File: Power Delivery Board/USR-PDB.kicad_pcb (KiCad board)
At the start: 2 copper layers, 110 x 150 mm, 40 parts, among them U1 XT90, U10 Anderson PP45 Vert. 2x1, U11 Anderson PP45 Vert. 2x1, U12 Anderson PP45 Vert. 2x1, U13 TL2575HV-05IKV, U14 MCP3002-I/P, U2 Anderson PP45 Vert. 2x1, U3 Anderson PP45 Vert. 2x1, U4 Anderson PP45 Vert. 2x1, U5 Anderson PP45 Vert. 2x1, U6 Anderson PP45 Vert. 2x1, U7 LM2676T-12_NOPB

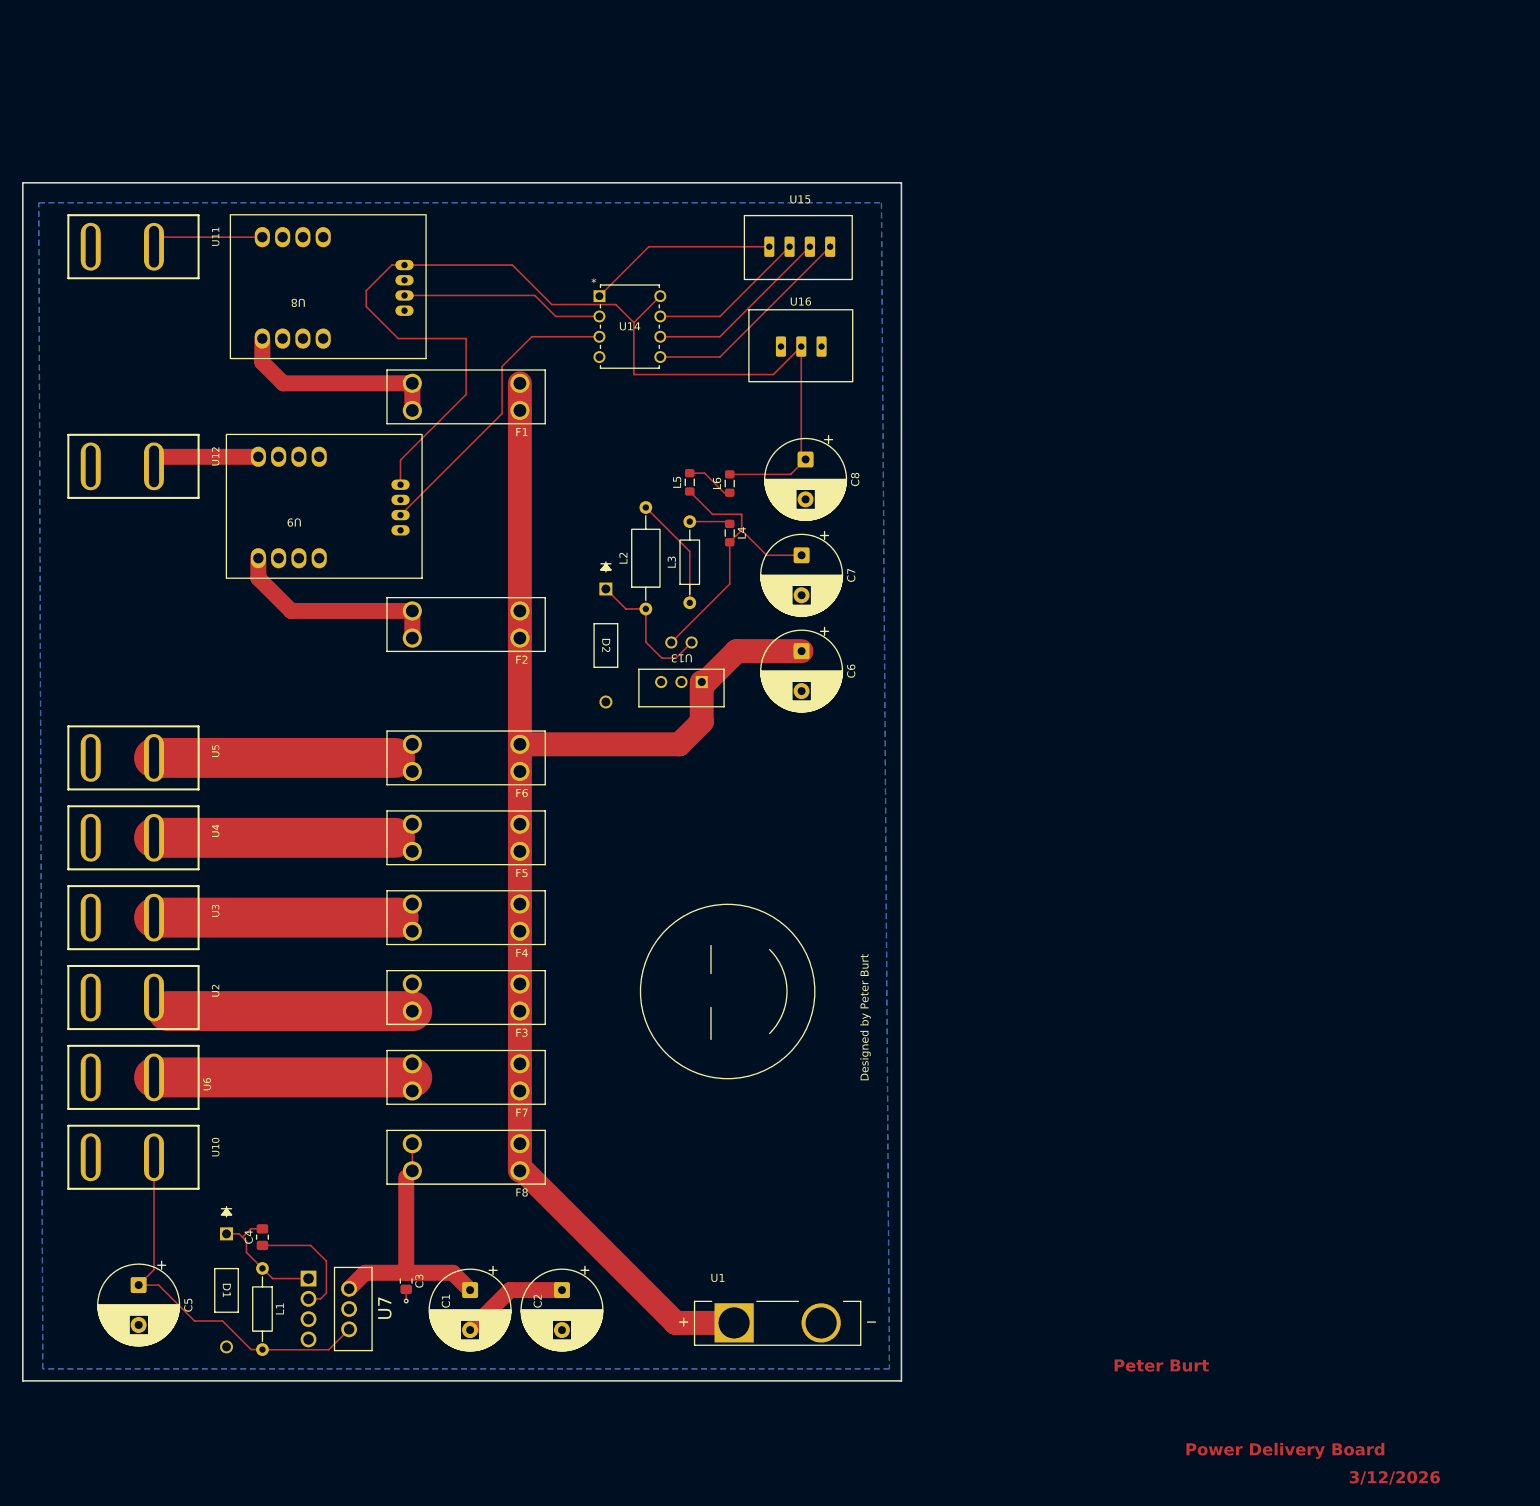
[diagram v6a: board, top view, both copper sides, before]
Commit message: Update PDB with easier-to-obtain components
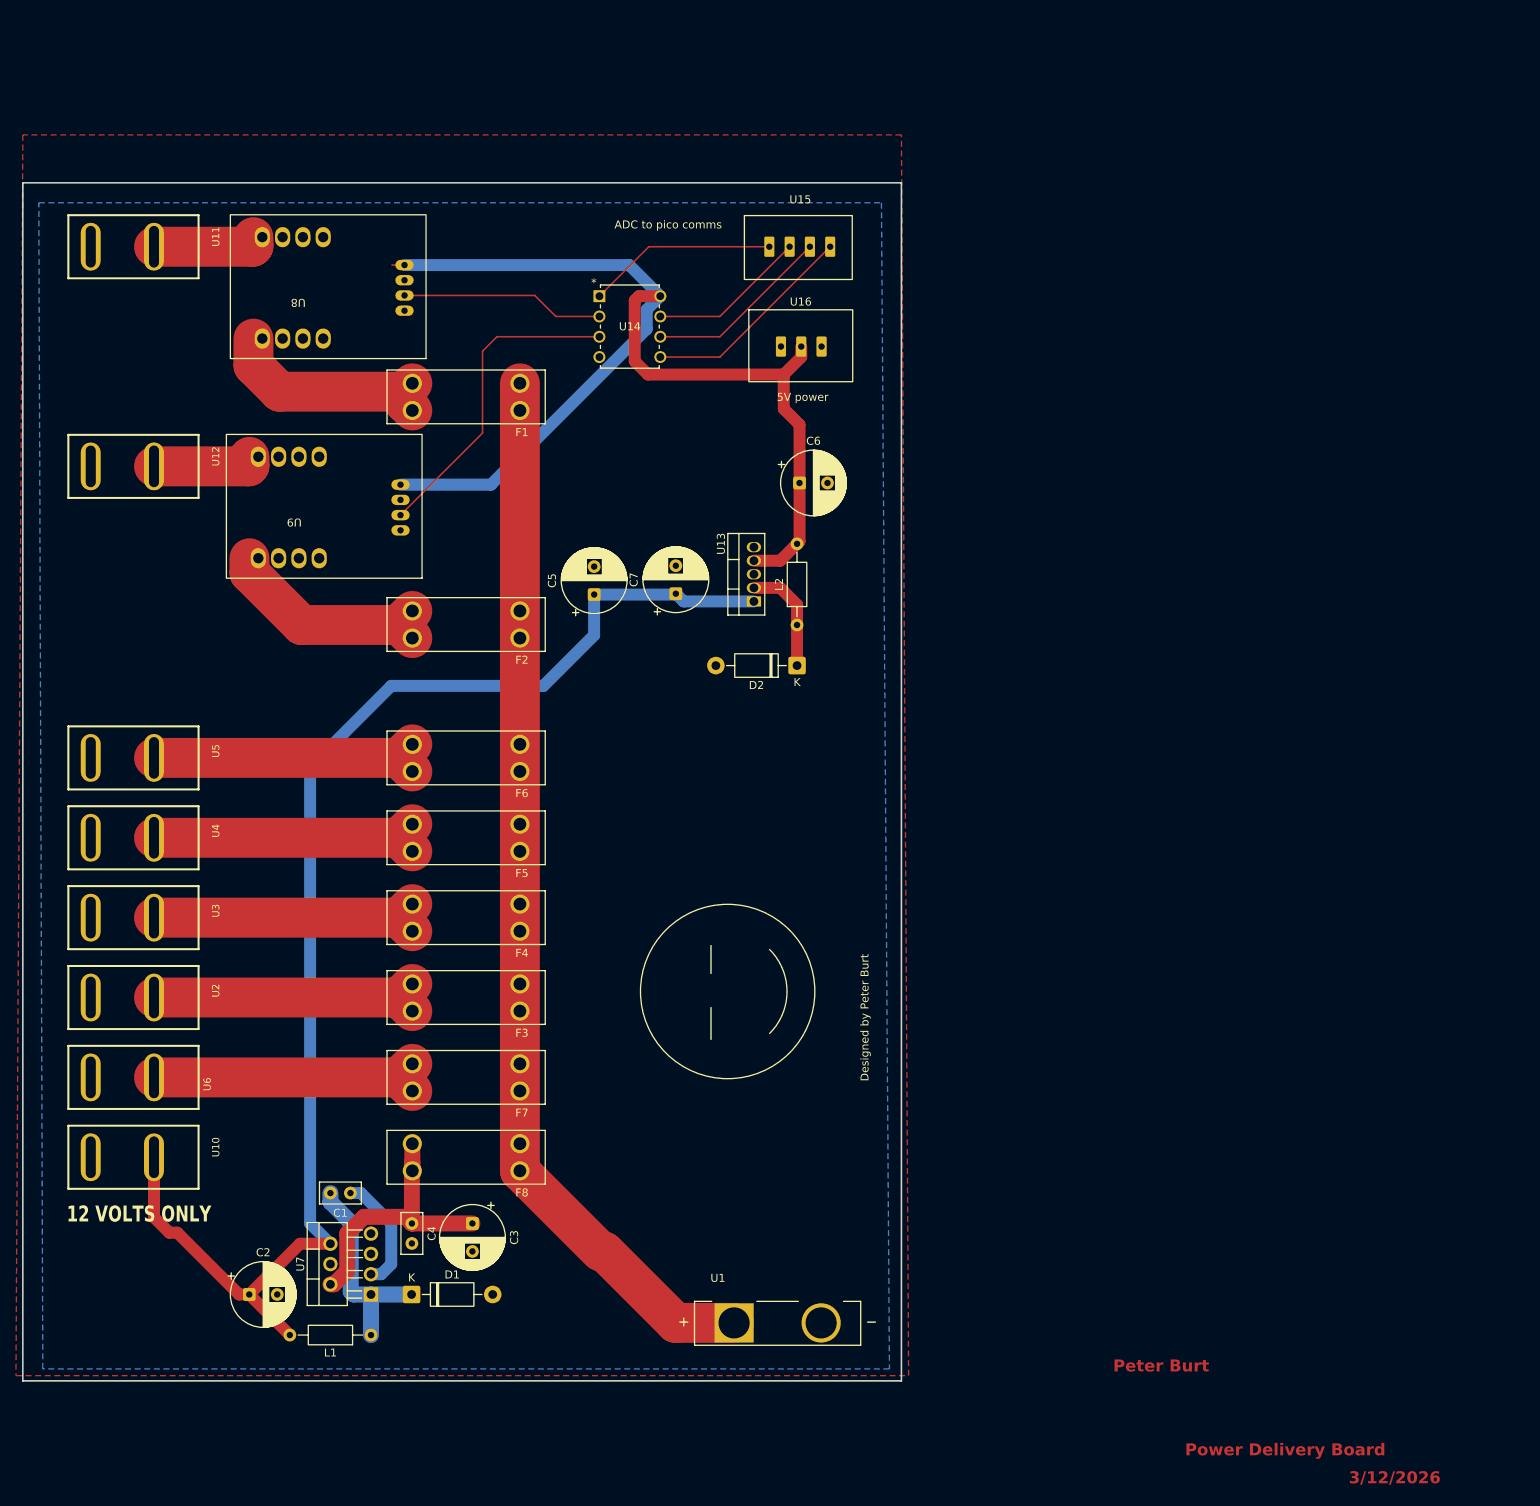
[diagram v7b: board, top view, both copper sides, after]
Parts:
- removed C8: 100uF, Capacitor_THT:CP_Radial_D10.0mm_P5.00mm
- removed L3: 100uH, Inductor_THT:L_Axial_L5.3mm_D2.2mm_P10.16mm_Horizontal_Vishay_IM-1
- removed L4, L5, L6: 10uH, Inductor_SMD:L_0805_2012Metric_Pad1.05x1.20mm_HandSolder
- C1: value 100uF -> 10nF; footprint Capacitor_THT:CP_Radial_D10.0mm_P5.00mm -> Capacitor_THT:C_Disc_D5.0mm_W2.5mm_P2.50mm
- C2: value 100uF -> 82uF; footprint Capacitor_THT:CP_Radial_D10.0mm_P5.00mm -> Capacitor_THT:CP_Radial_D8.0mm_P3.50mm
- C3: value 100nF -> 100uF; footprint Capacitor_SMD:C_0805_2012Metric_Pad1.18x1.45mm_HandSolder -> Capacitor_THT:CP_Radial_D8.0mm_P3.50mm
- C4: value 10nF -> 100uF; footprint Capacitor_SMD:C_0805_2012Metric_Pad1.18x1.45mm_HandSolder -> Capacitor_THT:C_Disc_D5.0mm_W2.5mm_P2.50mm
- C5: value 100uF -> 47uF; footprint Capacitor_THT:CP_Radial_D10.0mm_P5.00mm -> Capacitor_THT:CP_Radial_D8.0mm_P3.50mm
- C6: value 100uF -> 470uF; footprint Capacitor_THT:CP_Radial_D10.0mm_P5.00mm -> Capacitor_THT:CP_Radial_D8.0mm_P3.50mm
- C7: value 330uF -> 22uF; footprint Capacitor_THT:CP_Radial_D10.0mm_P5.00mm -> Capacitor_THT:CP_Radial_D8.0mm_P3.50mm
- D1: value 1N5821 -> SS24FL (550mV 2A); footprint USR:DO-41_STM -> Diode_THT:D_DO-41_SOD81_P10.16mm_Horizontal
- D2: value 1N5819 -> SS24FL (550mV 2A); footprint USR:DO-41_STM -> Diode_THT:D_DO-41_SOD81_P10.16mm_Horizontal
- L2: footprint Inductor_THT:L_Axial_L7.0mm_D3.3mm_P12.70mm_Horizontal_Fastron_MICC -> Inductor_THT:L_Axial_L5.3mm_D2.2mm_P10.16mm_Horizontal_Vishay_IM-1
- U13: value TL2575HV-05IKV -> LM2575-5.0BT; footprint USR:TL2575HV-05IKV -> Package_TO_SOT_THT:TO-220-5_Vertical
- U7: footprint USR:LM2676-TO127P457X1016X2052-7P -> Package_TO_SOT_THT:TO-220-7_P2.54x5.08mm_StaggerOdd_Lead3.08mm_Vertical
- moved C5 103.6 mm to (113.0, 82.5), turned to 90 degrees
- moved C2 39.2 mm to (69.8, 170.2), turned to 0 degrees
- moved D2 25.8 mm to (138.4, 91.4), turned to 180 degrees
- moved D1 24.4 mm to (90.2, 170.2), turned to 0 degrees
- moved C6 21.1 mm to (138.7, 68.6), turned to 0 degrees
- moved C1 19.3 mm to (82.5, 157.5), turned to 180 degrees
- moved L2 19.0 mm to (138.4, 86.4)
- moved C4 18.8 mm to (90.2, 161.3), turned to -90 degrees
- moved C7 16.5 mm to (123.3, 82.4), turned to 90 degrees
- moved U13 16.4 mm to (133.0, 83.4), turned to 90 degrees
- moved L1 15.9 mm to (85.1, 175.3), turned to 180 degrees
- moved C3 11.0 mm to (97.8, 161.3)
- moved U7 6.57 mm to (85.1, 170.2), turned to 90 degrees
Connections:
- C1 pad 1: Net-(U7-VIN) -> Net-(U7-BOOST)
- C1 pad 2: Net-(C1-Pad2) -> Net-(D1-K)
- C2 pad 1: Net-(C1-Pad2) -> /12V_OUT
- C4 pad 1: Net-(U7-BOOST) -> Net-(U7-VIN)
- C4 pad 2: Net-(D1-K) -> GND
- C5 pad 1: Net-(U10-VCC) -> /12V_OUT
- C6 pad 1: Vin -> /5V_OUT
- C7 pad 1: Net-(U13-FEEDBACK) -> /12V_OUT
- L1 pad 2: Net-(U10-VCC) -> /12V_OUT
- L2 pad 2: Net-(L2-Pad2) -> /5V_OUT
- U1 pad N: GND -> (no net)
- U1 pad P: Vin -> (no net)
- U10 pad 1: Net-(U10-VCC) -> /12V_OUT
- U13 pad 1: Vin -> /12V_OUT
- U13 pad 4: Net-(U13-FEEDBACK) -> /5V_OUT
- U14 pad 8: 5V -> /5V_OUT
- U16 pad 2: 5V -> /5V_OUT
- U7 pad 6: Net-(U10-VCC) -> /12V_OUT
- U8 pad 14: 5V -> /5V_OUT
- U9 pad 14: 5V -> /5V_OUT
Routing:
- net /12V_OUT: track 0.00 -> 172.1 mm
- net /5V_OUT: track 0.00 -> 142.1 mm
- net 5V: track 133.9 -> 0.00 mm
- net Net-(U10-VCC): track 48.1 -> 0.00 mm
- net Vin: track 176.3 -> 132.8 mm
- net Net-(U13-FEEDBACK): track 36.2 -> 0.00 mm
- net Net-(L2-Pad2): track 14.2 -> 0.00 mm
- net Net-(C1-Pad2): track 13.6 -> 0.00 mm
- net Net-(D1-K): track 16.3 -> 26.2 mm
- net Net-(L5-Pad2): track 6.01 -> 0.00 mm
- net Net-(L3-Pad2): track 5.12 -> 0.00 mm
- net Net-(D2-K): track 17.6 -> 13.9 mm
- net HE2_out: track 37.6 -> 40.2 mm
- net Net-(U2-VCC): track 36.4 -> 38.9 mm
- net Net-(U7-VIN): track 37.2 -> 35.4 mm
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- added copper zone on F.Cu, net GND
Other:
- board text added: "12 VOLTS ONLY"
- board text added: "5V power"
- board text added: "ADC to pico comms"

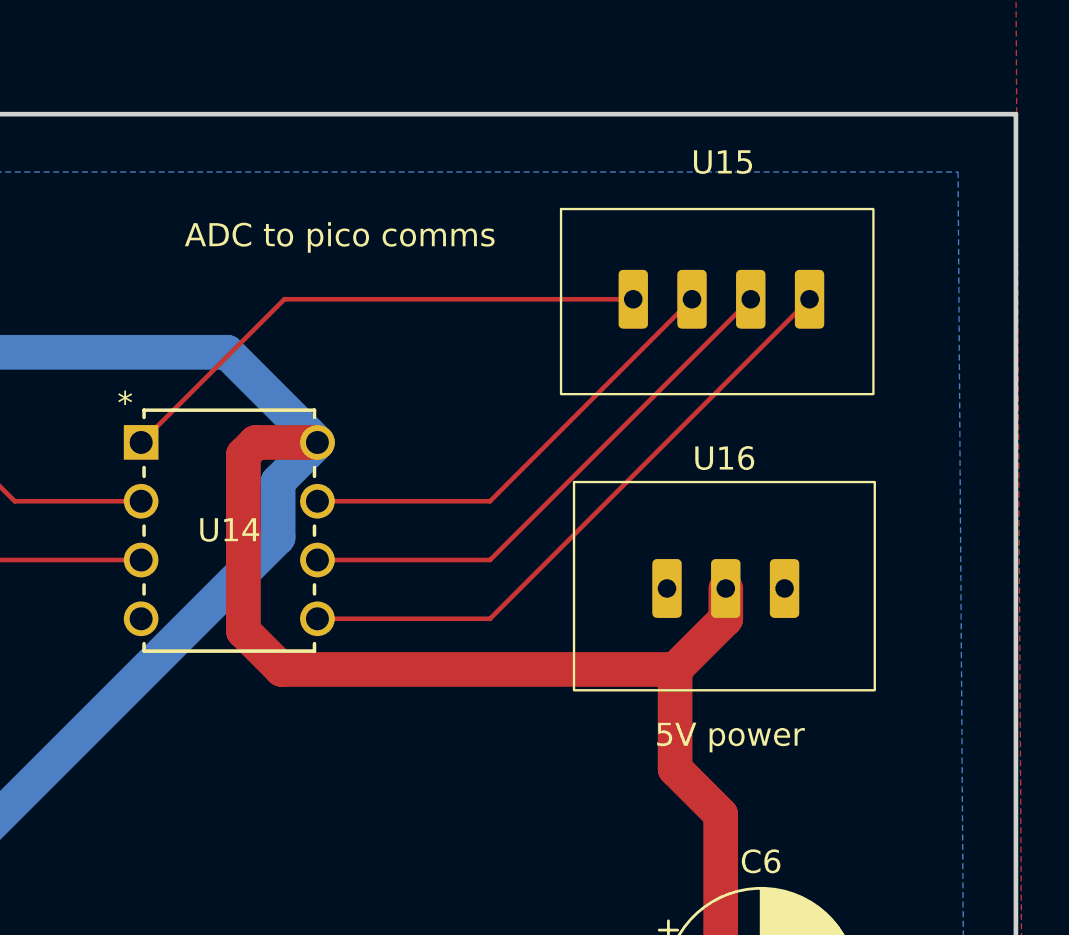
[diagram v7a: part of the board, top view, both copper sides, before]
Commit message: Changed JST connectors in the power delivery board's PCB to be RA JST connectors
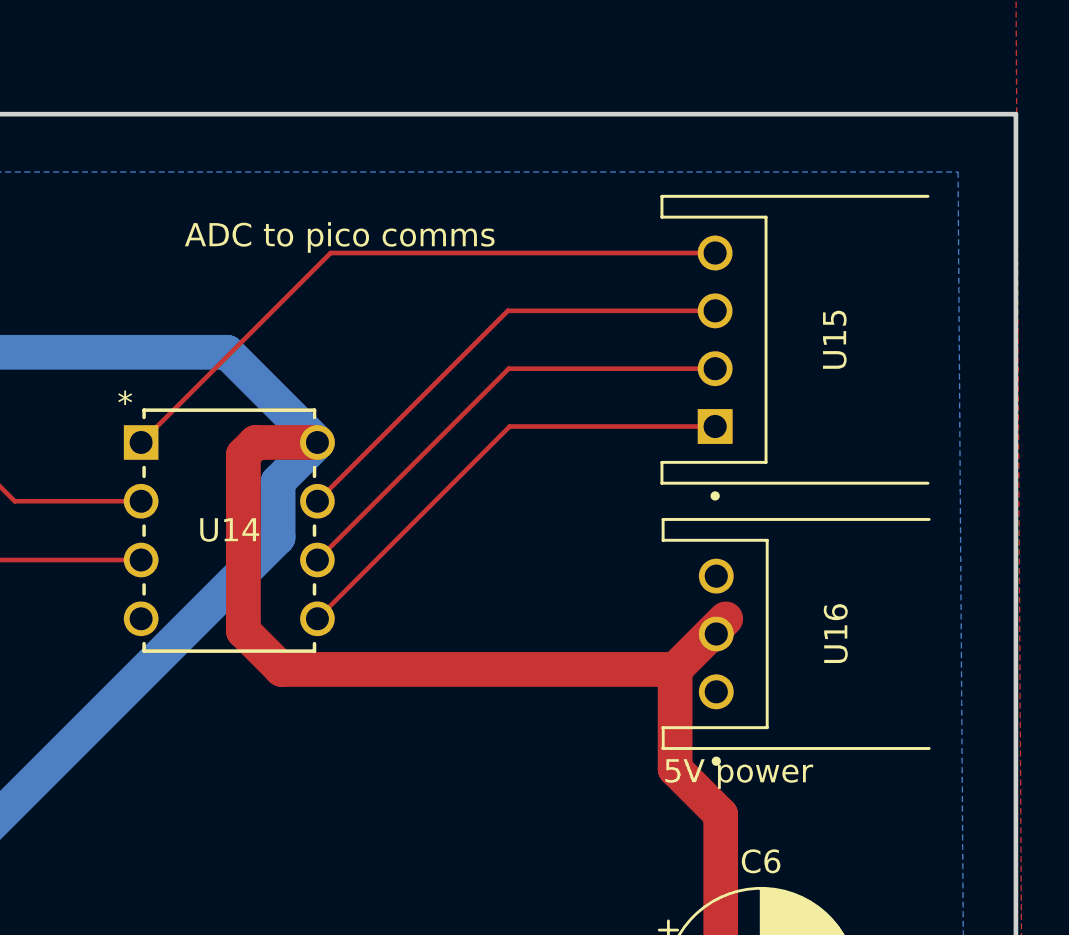
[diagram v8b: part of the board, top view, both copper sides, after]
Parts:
- moved U15 8.94 mm to (144.2, 40.8), turned to 90 degrees
- moved U16 8.86 mm to (144.2, 53.5), turned to 90 degrees
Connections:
- U15 pad 1: CS -> Din
- U15 pad 2: CLK -> Dout
- U15 pad 3: Dout -> CLK
- U15 pad 4: Din -> CS
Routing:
- net Din: track 27.0 -> 20.6 mm
- net CS: track 23.8 -> 28.2 mm
- net Dout: track 23.4 -> 20.6 mm
- net /5V_OUT: track 142.1 -> 140.8 mm
- net CLK: track 19.8 -> 20.6 mm
